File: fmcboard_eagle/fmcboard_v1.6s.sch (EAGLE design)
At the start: 281 parts, among them IC1 OPA699ID, IC10 LM358, IC11 7805DT, IC12 SN74AUC2G66DCTR, IC13 SN74AUC2G66DCTR, IC14 SN74AUC2G66DCTR, IC15 SN74AUC2G66DCTR, IC16 DAC7578SPWR, IC17 SN74AUC2G66DCTR, IC18 SN74AUC2G66DCTR, IC19 SN74AUC2G66DCTR, IC2 DAC7578SPWR, IC20 SN74AUC2G66DCTR, IC21 74AUP2GU04GW, IC22 74AUP2GU04GW, IC23 74AUP2GU04GW, IC24 74AUP2GU04GW, IC25 MC7905ACD2TR4G, IC26 AMS1117-1.8, IC27 LM358, IC28 SN74AUC2G66DCTR, IC29 LM337KVURG3, IC3 LTC6229IMS8E#TRPBF, IC30 SN74AUC2G66DCTR, IC31 SN74AUC2G66DCTR, IC32 SN74AUC2G66DCTR, IC33 LTC6229IMS8E#TRPBF, IC34 74AUP2GU04GW, IC35 74AUP2GU04GW, IC4 OPA695IDR, IC5 LTC6229IMS8E#TRPBF, IC6 OPA695IDR, IC7 OPA699ID, IC8 LM358, IC9 LM358, J1 8pin, J12 4p-2.54, J13 4p-2.54, J2 ASP-134604-01, J3 4p-2.54, J4 4p-2.54, J5 4p-2.54, J6 4p-2.54, J7 4p-2.54, J8 4p-2.54

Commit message: and power +-7 onboard laid out
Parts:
- removed C110, C111, C112, C113, C114, C115: 10uF, passives:CAPACITOR0402_CAP
- removed J4, J6, J7: 4p-2.54, Seeed-Connector:DIP-BLACK-FEMALE-HEADER-VERT(4P-2.54)
- added C11, C121, C8: 0.1uF, passives:CAPACITOR0402_CAP
- added C118, C119, C120, C64, C80: 10uF, passives:CAPACITOR0402_CAP
- added C122: 0.01uF, passives:CAPACITOR0402_CAP
- added C123, C124, C125: 100uF, rcl:C-EUC1206K
- added D1, D2: B340A, SparkFun-DiscreteSemi:DIODE-SCHOTTKY-B340A
- added IC36, IC37: TPS5430DDAR, TPS5430DDAR:TPS5430DDAR
- added J9: 2p-2.54, Seeed-Connector:DIP-BLACK-MALE-HEADER-VERT(2P-2.54)
- added L3, L4: 10uH, SparkFun-Passives:INDUCTORPWR
- added R116, R117, R60, R84: 1k, passives:RESISTOR0402_RES
- added R118, R73: 10k, passives:RESISTOR0402_RES
- C106: value 10uF -> 0.1uF
- C107: value 10uF -> 0.01uF
- C108, C109: value 10uF -> 100uF; device passives:CAPACITOR0402_CAP -> rcl:C-EUC1206K
- J3: value 4p-2.54 -> 2p-2.54; device Seeed-Connector:DIP-BLACK-FEMALE-HEADER-VERT(4P-2.54) -> Seeed-Connector:DIP-BLACK-MALE-HEADER-VERT(2P-2.54)
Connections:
- new net ARVIN: ARDUINO_NANO1.VIN
- new net BOOT1: C122.1, IC37.BOOT
- new net BOOT2: C107.1, IC36.BOOT
- new net FB1: IC37.VSENSE, R60.2, R73.1
- new net FB2: IC36.VSENSE, R116.2, R118.1
- new net N$29: C120.1, C64.2
- new net N$36: J5.P$2, R72.1
- new net N$39: C119.2, C41.1
- new net N$52: C120.2, C80.1
- new net N$53: C123.1, C124.2
- new net N$54: R60.1, R84.2
- new net N$55: C108.1, C109.2
- new net N$56: R116.1, R117.2
- new net SW1: C122.2, D1.C, IC37.PH, L3.1
- new net SW2: C107.2, D2.C, IC36.PH, L4.1
- new net V-: IC36.EP, IC36.GND
- new net VIN: C11.1, C64.1, C8.1, IC36.VIN, IC37.VIN, J9.2
- net 12V: now also J9.1; no longer J8.P$2, J8.P$3, J8.P$4
- net 1V8-: now also C125.1; no longer C106.1, C107.1, C108.1, C109.1, C110.1, C111.1, C112.1, C113.1, C114.1, C115.1
- net 3V3: now also J8.P$4; no longer J3.P$1, J3.P$2, J3.P$3, J3.P$4
- net GND: now also C106.1, C109.1, C11.2, C119.1, C121.2, C123.2, C125.2, C8.2, C80.2, D1.A, IC37.EP, IC37.GND, J3.1, J3.2, L4.2, R118.2, R84.1; no longer C106.2, C107.2, C108.2, C109.2, C110.2, C111.2, C112.2, C113.2, C114.2, C115.2, C41.1, J4.P$1, J4.P$2, J4.P$3, J4.P$4, J5.P$2
- net N$38: now also C1.1, C118.2; no longer J13.P$4, R72.1
- net OP1BUF: now also R72.2; no longer R89.2
- net PULSESUMIN: now also J13.P$4
- net TRANSOUT: now also R89.2; no longer R72.2
- net VIN+: now also C118.1, C121.1, C124.1, L3.2, R73.2; no longer C1.1
- net VIN-: now also C106.2, C108.2, D2.A, R117.1
- net VS+: now also J8.P$2; no longer J6.P$1, J6.P$2, J6.P$3, J6.P$4
- net VS-: now also J8.P$3; no longer J7.P$1, J7.P$2, J7.P$3, J7.P$4
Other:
- note added: "Vout = (R1/R2 +1) * 1.221 V = (10/2 + 1) * 1.221 V = 7.3 V"
- note removed: "10*10uF=100uF"

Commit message: 1.65s
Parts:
- R9: value 1-3k -> 1?-3?k
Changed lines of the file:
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@@
 <part name="SUPPLY125" library="supply2" library_urn="urn:adsk.eagle:library:372" deviceset="GND" device=""/>
 <part name="IC1" library="OPA699ID" deviceset="OPA699ID" device=""/>
-<part name="R9" library="passives" deviceset="RESISTOR" device="0402_RES" value="1-3k"/>
+<part name="R9" library="passives" deviceset="RESISTOR" device="0402_RES" value="1?-3?k"/>
 <part name="R10" library="passives" deviceset="RESISTOR" device="0402_RES" value="100"/>
 <part name="SUPPLY1" library="supply2" library_urn="urn:adsk.eagle:library:372" deviceset="GND" device=""/>

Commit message: remove LCSC 17415 0805 bug
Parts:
- R13, R3, R71, R72, R86, R88, R89: LCSC C17415 -> (none)
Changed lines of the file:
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@@
 </pinmapping>
 </spice>
-<attribute name="LCSC" value="C17415"/>
 </part>
 <part name="SUPPLY18" library="supply2" library_urn="urn:adsk.eagle:library:372" deviceset="GND" device=""/>
@@
 </pinmapping>
 </spice>
-<attribute name="LCSC" value="C17415"/>
 </part>
 <part name="SUPPLY21" library="supply2" library_urn="urn:adsk.eagle:library:372" deviceset="GND" device=""/>
@@
 </pinmapping>
 </spice>
-<attribute name="LCSC" value="C17415"/>
 </part>
 <part name="R72" library="passives" deviceset="RESISTOR" device="0402_RES" value="10">
@@
 </pinmapping>
 </spice>
-<attribute name="LCSC" value="C17415"/>
 </part>
 <part name="R86" library="passives" deviceset="RESISTOR" device="0402_RES" value="10">
@@
 </pinmapping>
 </spice>
-<attribute name="LCSC" value="C17415"/>
 </part>
 <part name="R88" library="passives" deviceset="RESISTOR" device="0402_RES" value="10">
@@
 </pinmapping>
 </spice>
-<attribute name="LCSC" value="C17415"/>
 </part>
 <part name="J5" library="Seeed-Connector" library_urn="urn:adsk.eagle:library:478" deviceset="DIP-BLACK-FEMALE-HEADER-VERT(4P-2.54)" device="" package3d_urn="urn:adsk.eagle:package:33137/1" value="4p-2.54"/>
@@
 </pinmapping>
 </spice>
-<attribute name="LCSC" value="C17415"/>
 </part>
 <part name="SUPPLY125" library="supply2" library_urn="urn:adsk.eagle:library:372" deviceset="GND" device=""/>

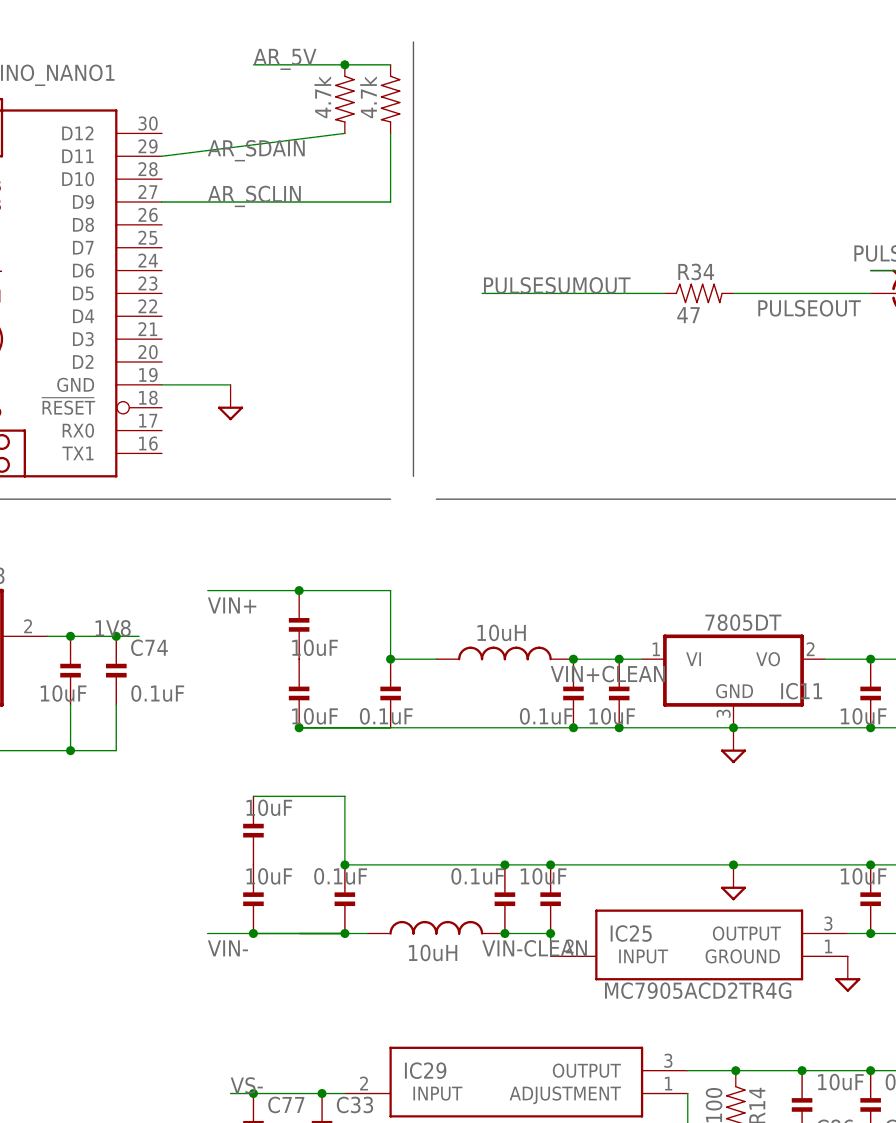
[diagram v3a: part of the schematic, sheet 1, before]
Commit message: extra 10 uF caps
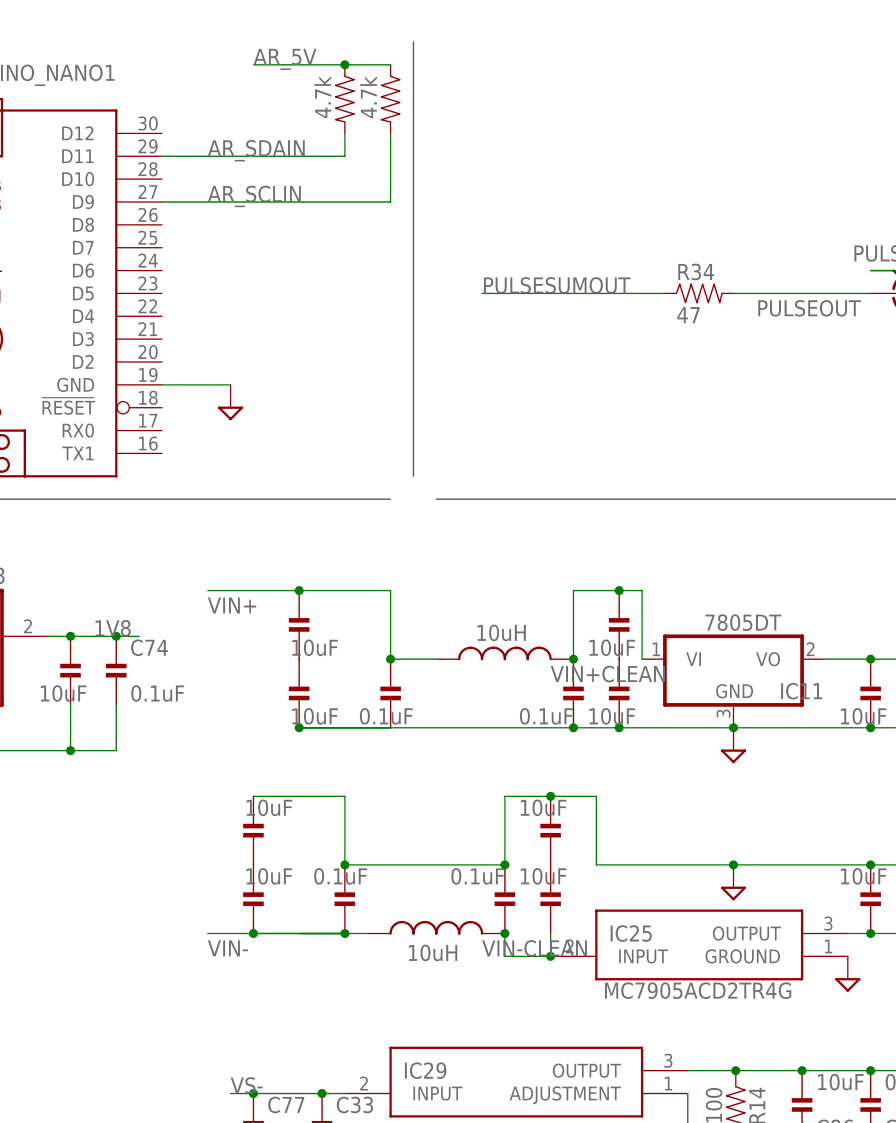
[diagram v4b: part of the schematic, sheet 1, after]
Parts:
- added C110, C111: 10uF, passives:CAPACITOR0402_CAP
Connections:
- new net N$58: C110.1, C2.2
- new net N$59: C111.1, C40.2
- net GND: now also C110.2; no longer C2.2
- net VIN-CLEAN: now also C111.2; no longer C40.2
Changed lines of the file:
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@@
 <part name="C106" library="passives" deviceset="CAPACITOR" device="0402_CAP" value="0.1uF"/>
 <part name="GND3" library="SparkFun-PowerSymbols" library_urn="urn:adsk.eagle:library:530" deviceset="GND" device=""/>
+<part name="C110" library="passives" deviceset="CAPACITOR" device="0402_CAP" value="10uF"/>
+<part name="C111" library="passives" deviceset="CAPACITOR" device="0402_CAP" value="10uF"/>
 </parts>
 <sheets>
@@
 <attribute name="VALUE" x="-11.176" y="30.861" size="1.778" layer="96"/>
 </instance>
-<instance part="C2" gate="G$1" x="25.4" y="35.56" smashed="yes">
-<attribute name="VALUE" x="21.844" y="30.861" size="1.778" layer="96"/>
+<instance part="C2" gate="G$1" x="25.4" y="43.18" smashed="yes">
+<attribute name="VALUE" x="21.844" y="38.481" size="1.778" layer="96"/>
 </instance>
 <instance part="C38" gate="G$1" x="53.34" y="35.56" smashed="yes">
@@
 <attribute name="VALUE" x="49.784" y="13.081" size="1.778" layer="96"/>
 </instance>
-<instance part="C40" gate="G$1" x="17.78" y="12.7" smashed="yes">
-<attribute name="VALUE" x="14.224" y="13.081" size="1.778" layer="96"/>
+<instance part="C40" gate="G$1" x="17.78" y="20.32" smashed="yes">
+<attribute name="VALUE" x="14.224" y="20.701" size="1.778" layer="96"/>
 </instance>
 <instance part="C41" gate="G$1" x="-15.24" y="12.7" smashed="yes">
@@
 <attribute name="NAME" x="57.15" y="-21.59" size="1.778" layer="95" rot="R90" align="center-left"/>
 <attribute name="VALUE" x="64.77" y="-21.59" size="1.778" layer="96" rot="R90" align="center-left"/>
+</instance>
+<instance part="C110" gate="G$1" x="25.4" y="35.56" smashed="yes">
+<attribute name="VALUE" x="21.844" y="30.861" size="1.778" layer="96"/>
+</instance>
+<instance part="C111" gate="G$1" x="17.78" y="12.7" smashed="yes">
+<attribute name="VALUE" x="14.224" y="13.081" size="1.778" layer="96"/>
 </instance>
 </instances>
@@
 <segment>
 <pinref part="SUPPLY31" gate="GND" pin="GND"/>
+<junction x="38.1" y="30.48"/>
+<pinref part="C47" gate="G$1" pin="2"/>
 <wire x1="58.42" y1="30.48" x2="53.34" y2="30.48" width="0.1524" layer="91"/>
-<junction x="38.1" y="30.48"/>
+<pinref part="C38" gate="G$1" pin="2"/>
+<junction x="53.34" y="30.48"/>
 <wire x1="53.34" y1="30.48" x2="38.1" y2="30.48" width="0.1524" layer="91"/>
+<pinref part="IC11" gate="A1" pin="GND"/>
+<pinref part="C110" gate="G$1" pin="2"/>
+<wire x1="38.1" y1="30.48" x2="25.4" y2="30.48" width="0.1524" layer="91"/>
 <wire x1="0" y1="30.48" x2="-10.16" y2="30.48" width="0.1524" layer="91"/>
 <wire x1="-10.16" y1="30.48" x2="20.32" y2="30.48" width="0.1524" layer="91"/>
-<wire x1="20.32" y1="30.48" x2="25.4" y2="30.48" width="0.1524" layer="91"/>
 <pinref part="C43" gate="G$1" pin="2"/>
-<junction x="20.32" y="30.48"/>
-<pinref part="C47" gate="G$1" pin="2"/>
 <pinref part="C42" gate="G$1" pin="2"/>
 <pinref part="C1" gate="G$1" pin="2"/>
 <junction x="-10.16" y="30.48"/>
-<pinref part="C2" gate="G$1" pin="2"/>
-<wire x1="25.4" y1="30.48" x2="38.1" y2="30.48" width="0.1524" layer="91"/>
+<wire x1="25.4" y1="30.48" x2="20.32" y2="30.48" width="0.1524" layer="91"/>
 <junction x="25.4" y="30.48"/>
-<pinref part="C38" gate="G$1" pin="2"/>
-<junction x="53.34" y="30.48"/>
-<pinref part="IC11" gate="A1" pin="GND"/>
+<junction x="20.32" y="30.48"/>
 </segment>
 <segment>
@@
 <junction x="38.1" y="15.24"/>
 <wire x1="53.34" y1="15.24" x2="38.1" y2="15.24" width="0.1524" layer="91"/>
-<wire x1="38.1" y1="15.24" x2="17.78" y2="15.24" width="0.1524" layer="91"/>
+<wire x1="38.1" y1="15.24" x2="22.86" y2="15.24" width="0.1524" layer="91"/>
+<wire x1="22.86" y1="15.24" x2="22.86" y2="22.86" width="0.1524" layer="91"/>
+<wire x1="22.86" y1="22.86" x2="17.78" y2="22.86" width="0.1524" layer="91"/>
 <pinref part="C45" gate="G$1" pin="1"/>
-<wire x1="17.78" y1="15.24" x2="12.7" y2="15.24" width="0.1524" layer="91"/>
+<wire x1="17.78" y1="22.86" x2="12.7" y2="22.86" width="0.1524" layer="91"/>
+<wire x1="12.7" y1="22.86" x2="12.7" y2="15.24" width="0.1524" layer="91"/>
 <pinref part="C46" gate="G$1" pin="1"/>
 <pinref part="C39" gate="G$1" pin="1"/>
 <junction x="53.34" y="15.24"/>
 <pinref part="C40" gate="G$1" pin="1"/>
-<junction x="17.78" y="15.24"/>
+<junction x="17.78" y="22.86"/>
 <pinref part="C44" gate="G$1" pin="1"/>
 <wire x1="-5.08" y1="15.24" x2="-5.08" y2="22.86" width="0.1524" layer="91"/>
@@
 <net name="AR_SDAIN" class="0">
 <segment>
-<wire x1="-25.4" y1="93.98" x2="-5.08" y2="96.52" width="0.1524" layer="91"/>
+<wire x1="-25.4" y1="93.98" x2="-5.08" y2="93.98" width="0.1524" layer="91"/>
+<wire x1="-5.08" y1="93.98" x2="-5.08" y2="96.52" width="0.1524" layer="91"/>
 <label x="-20.32" y="93.98" size="1.778" layer="95"/>
 <pinref part="ARDUINO_NANO1" gate="G$1" pin="D11"/>
@@
 <net name="VIN+CLEAN" class="1">
 <segment>
-<wire x1="27.94" y1="38.1" x2="25.4" y2="38.1" width="0.1524" layer="91"/>
+<wire x1="27.94" y1="38.1" x2="27.94" y2="45.72" width="0.1524" layer="91"/>
+<wire x1="27.94" y1="45.72" x2="25.4" y2="45.72" width="0.1524" layer="91"/>
 <pinref part="L1" gate="G$1" pin="2"/>
 <junction x="20.32" y="38.1"/>
-<wire x1="20.32" y1="38.1" x2="25.4" y2="38.1" width="0.1524" layer="91"/>
+<wire x1="20.32" y1="38.1" x2="20.32" y2="45.72" width="0.1524" layer="91"/>
+<wire x1="20.32" y1="45.72" x2="25.4" y2="45.72" width="0.1524" layer="91"/>
 <pinref part="C43" gate="G$1" pin="1"/>
 <label x="17.78" y="35.56" size="1.778" layer="95"/>
 <pinref part="C2" gate="G$1" pin="1"/>
-<junction x="25.4" y="38.1"/>
+<junction x="25.4" y="45.72"/>
 <pinref part="IC11" gate="A1" pin="VI"/>
 </segment>
@@
 <net name="VIN-CLEAN" class="1">
 <segment>
+<label x="10.16" y="5.08" size="1.778" layer="95"/>
+<pinref part="IC25" gate="G$1" pin="INPUT"/>
+<wire x1="12.7" y1="7.62" x2="12.7" y2="5.08" width="0.1524" layer="91"/>
+<wire x1="12.7" y1="5.08" x2="17.78" y2="5.08" width="0.1524" layer="91"/>
 <pinref part="L2" gate="G$1" pin="2"/>
+<pinref part="C45" gate="G$1" pin="2"/>
 <junction x="12.7" y="7.62"/>
-<wire x1="12.7" y1="7.62" x2="17.78" y2="7.62" width="0.1524" layer="91"/>
-<pinref part="C45" gate="G$1" pin="2"/>
-<label x="10.16" y="5.08" size="1.778" layer="95"/>
-<pinref part="C40" gate="G$1" pin="2"/>
-<junction x="17.78" y="7.62"/>
-<pinref part="IC25" gate="G$1" pin="INPUT"/>
+<pinref part="C111" gate="G$1" pin="2"/>
 <wire x1="17.78" y1="7.62" x2="17.78" y2="5.08" width="0.1524" layer="91"/>
+<junction x="17.78" y="5.08"/>
 </segment>
 </net>
@@
 </segment>
 </net>
+<net name="N$58" class="0">
+<segment>
+<pinref part="C2" gate="G$1" pin="2"/>
+<pinref part="C110" gate="G$1" pin="1"/>
+</segment>
+</net>
+<net name="N$59" class="0">
+<segment>
+<pinref part="C40" gate="G$1" pin="2"/>
+<pinref part="C111" gate="G$1" pin="1"/>
+</segment>
+</net>

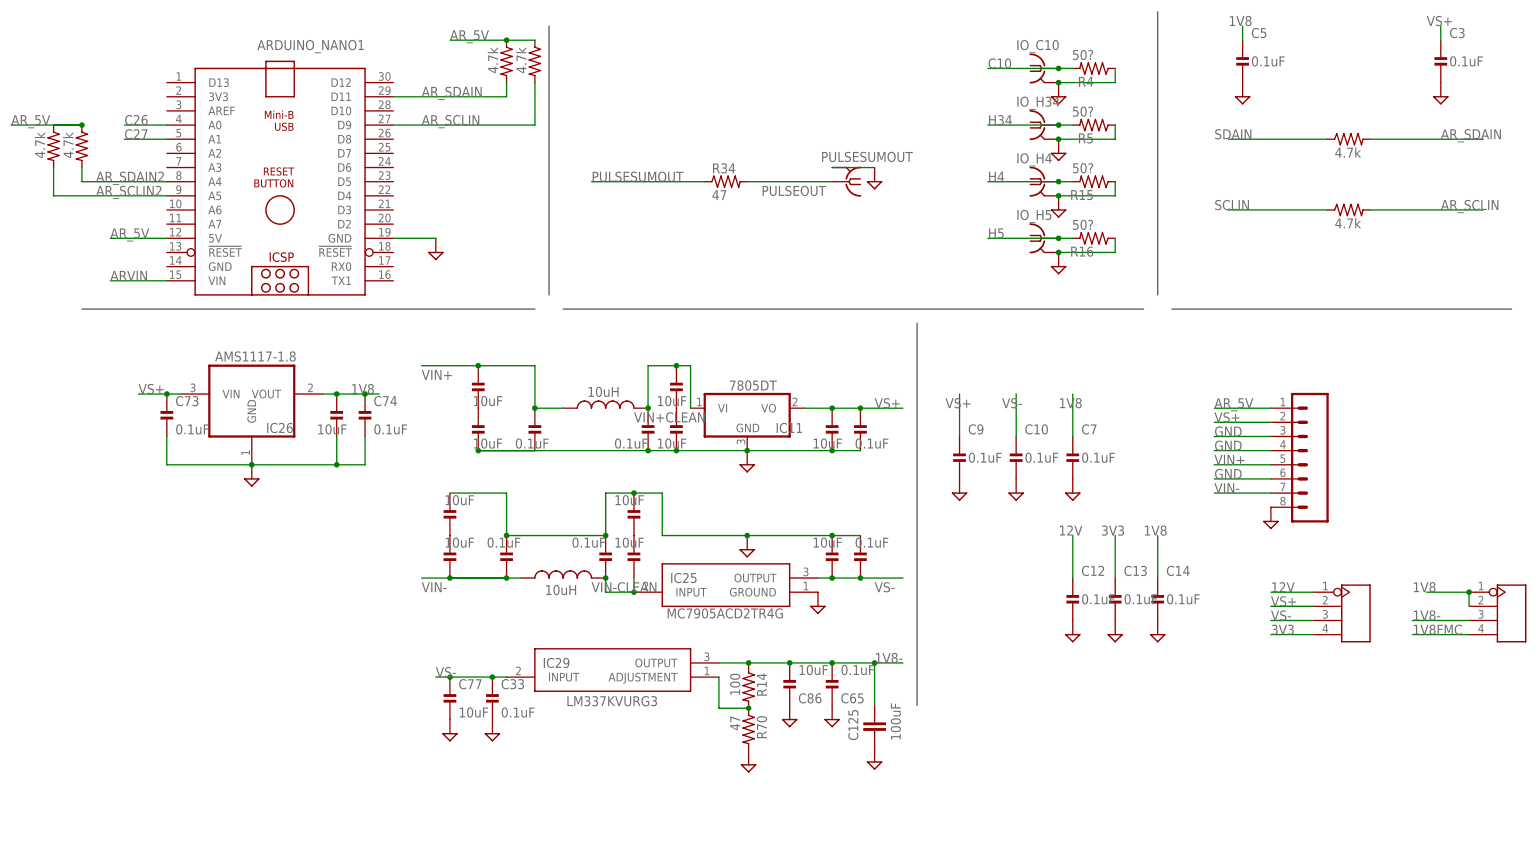
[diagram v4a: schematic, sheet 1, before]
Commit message: v1.652s Add C18 C19 C22 C23 pulse out holes Add C26 C27 SDAIN SCLIN holes
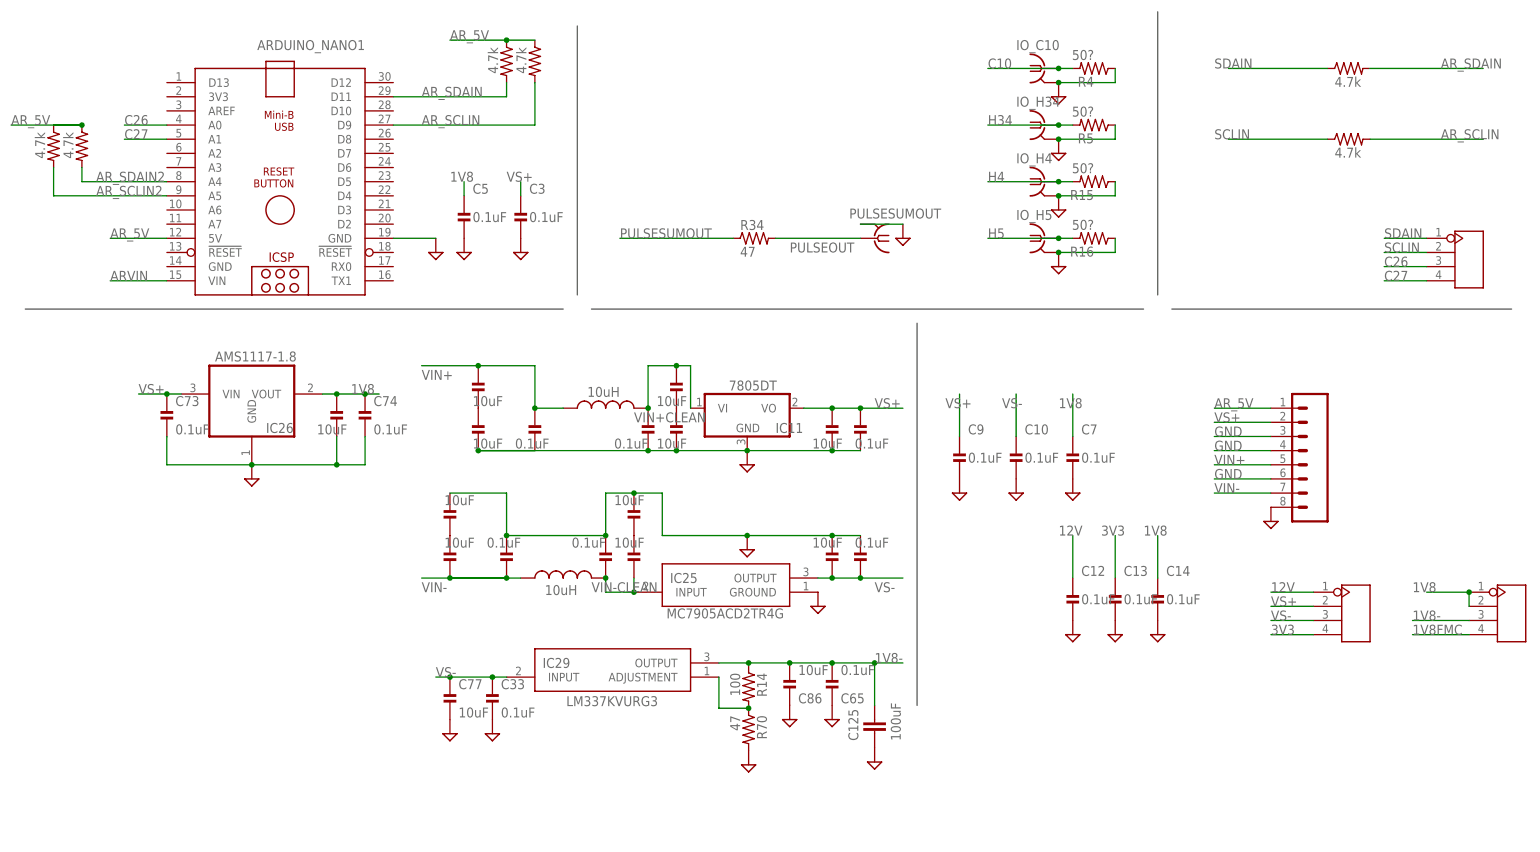
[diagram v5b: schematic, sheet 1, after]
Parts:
- added J4: 4p-2.54, Seeed-Connector:DIP-BLACK-FEMALE-HEADER-VERT(4P-2.54)
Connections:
- net C18: now also SV2.19
- net C19: now also SV2.20
- net C22: now also SV1.1
- net C23: now also SV1.2
- net C26: now also J4.P$3
- net C27: now also J4.P$4
- net GND: no longer SV2.19, SV2.20
- net SCLIN: now also J4.P$2; no longer SV1.1
- net SDAIN: now also J4.P$1; no longer SV1.2
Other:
- moved on the sheet: C3, C5, PULSESUMOUT, R34
